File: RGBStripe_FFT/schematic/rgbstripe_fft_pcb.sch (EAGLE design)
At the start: 15 parts, among them IC1 MSGEQ7P, M1 ARDUINO-NANO-3.0

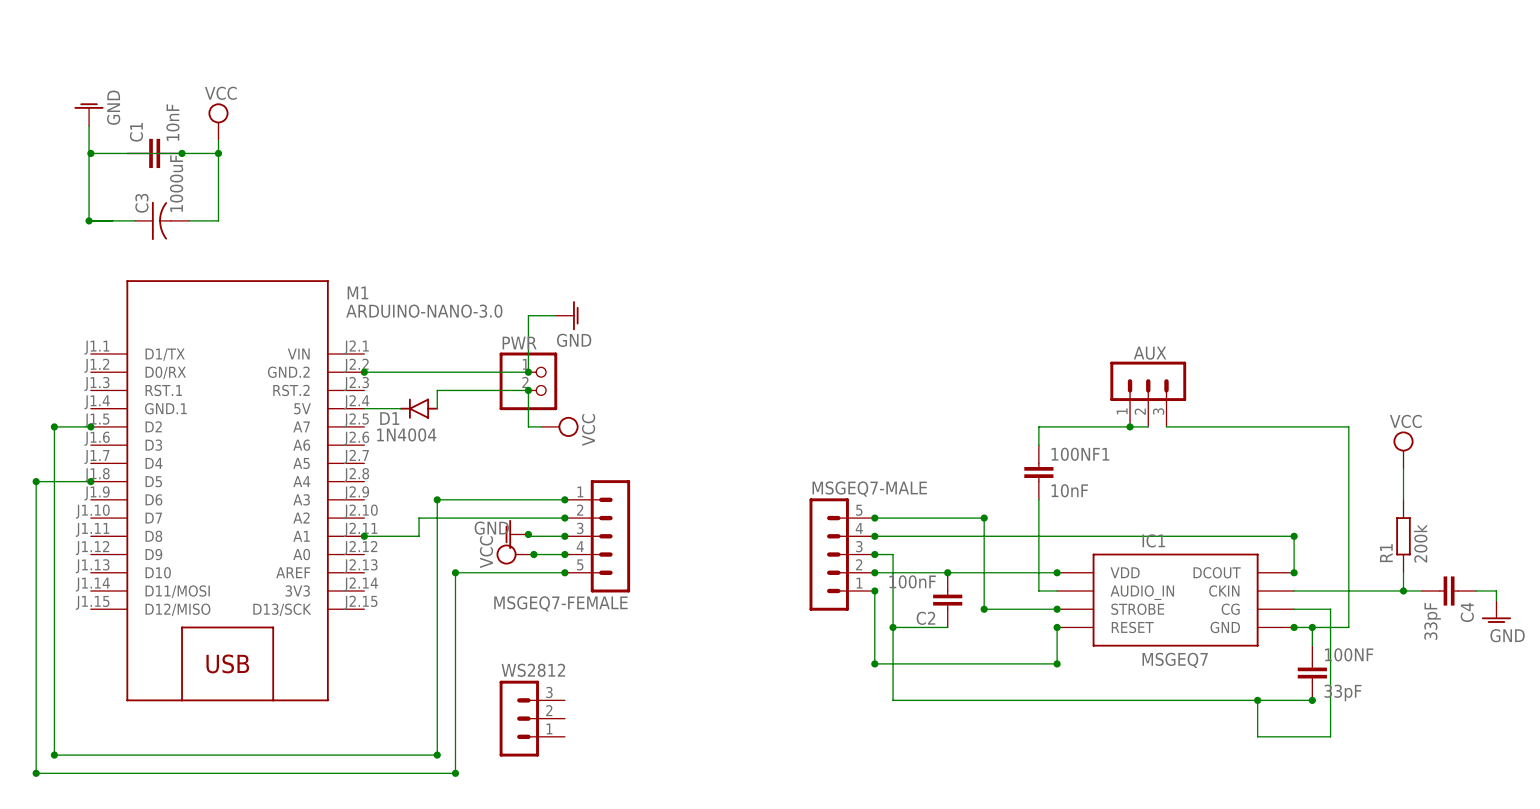
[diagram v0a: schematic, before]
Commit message: added Sketch + Schematic using FFT instead of MSGEQ7 Circuit
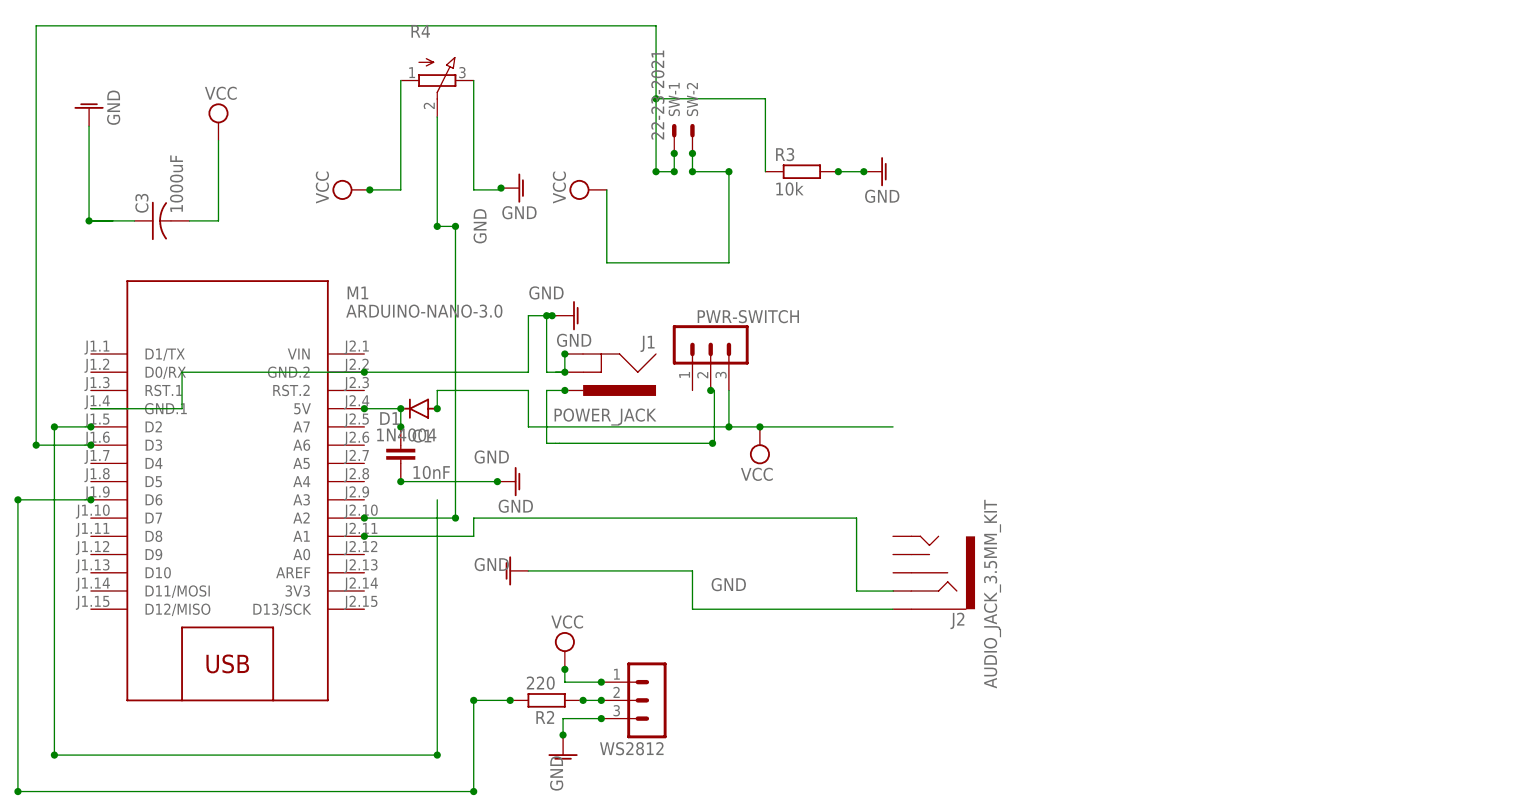
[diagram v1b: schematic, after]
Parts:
- removed 100NF, C4: 33pF, resistor:C-EU025-025X050
- removed 100NF1: 10nF, resistor:C-EU025-025X050
- removed AUX: (no value), con-lstb:MA03-1
- removed C2: 100nF, resistor:C-EU025-025X050
- removed IC1: MSGEQ7P, SparkFun-IC-Special-Function:MSGEQ7DIL
- removed MSGEQ7-FEMALE, MSGEQ7-MALE: (no value), con-lstb:MA05-1
- removed PWR: (no value), pinhead:PINHD-1X2
- removed R1: 200k, resistor:R-EU_0204/5
- added J1: POWER_JACK, SparkFun-Connectors:POWER_JACK
- added J2: AUDIO_JACK_3.5MM_KIT, SparkFun-Connectors:AUDIO_JACK_3.5MM_KIT
- added PWR-SWITCH: (no value), con-lstb:MA03-1
- added R2: 220, resistor:R-EU_0204/5
- added R3: 10k, resistor:R-EU_0204/5
- added R4: (no value), pot:3RP/1610N
- added SW: 22-23-2021, con-molex:22-23-2021
- M1: device diy-modules:ARDUINO-NANO-3.0 -> diy-modules-nano:ARDUINO-NANO-3.0
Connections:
- removed net GNDA: C3.1, C4.1, M1.GND.2, MSGEQ7-FEMALE.3, PWR.1
- removed net N$10: 100NF1.1, AUX.1, AUX.2
- removed net N$11: C4.2, IC1.CKIN, R1.1
- removed net N$12: 100NF.1, AUX.3, IC1.GND
- removed net N$13: 100NF1.2, IC1.AUDIO_IN
- removed net N$2: M1.D5, MSGEQ7-FEMALE.5
- removed net N$3: M1.A1, MSGEQ7-FEMALE.2
- removed net N$4: M1.D2, MSGEQ7-FEMALE.1
- removed net N$5: C2.2, IC1.VDD, MSGEQ7-MALE.2
- removed net N$7: IC1.DCOUT, MSGEQ7-MALE.4
- removed net N$9: IC1.RESET, MSGEQ7-MALE.1
- new net GND: C1.2, C3.1, J1.GND, J1.GNDBREAK, J2.SLEEVE, M1.GND.1, M1.GND.2, R3.2, R4.E, WS2812.3
- new net N$14: M1.D6, R2.2
- new net N$15: M1.A2, R4.S
- new net N$16: R2.1, WS2812.2
- new net N$17: M1.D3, R3.1, SW-1.S
- new net N$19: J1.PWR, PWR-SWITCH.2
- net N$1: now also C1.1
- net N$6: now also J2.RING, M1.A1; no longer 100NF.2, C2.1, IC1.CG, MSGEQ7-MALE.3
- net N$8: now also M1.D2; no longer IC1.STROBE, MSGEQ7-MALE.5
- net VCC: now also PWR-SWITCH.3, R4.A, SW-2.S, WS2812.1; no longer C1.1, C1.2, MSGEQ7-FEMALE.4, PWR.2, R1.2
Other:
- moved on the sheet: C1, WS2812
